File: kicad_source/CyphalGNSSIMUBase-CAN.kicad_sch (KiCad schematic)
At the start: 24 parts, among them CN1 RASPBERRYPI_PICO, CN2 SM04B-SRSS-TB, CN3 SM04B-SRSS-TB, SW1 PTS636 SM43 SMTR LFS, U3 M24C64-RMN6TP

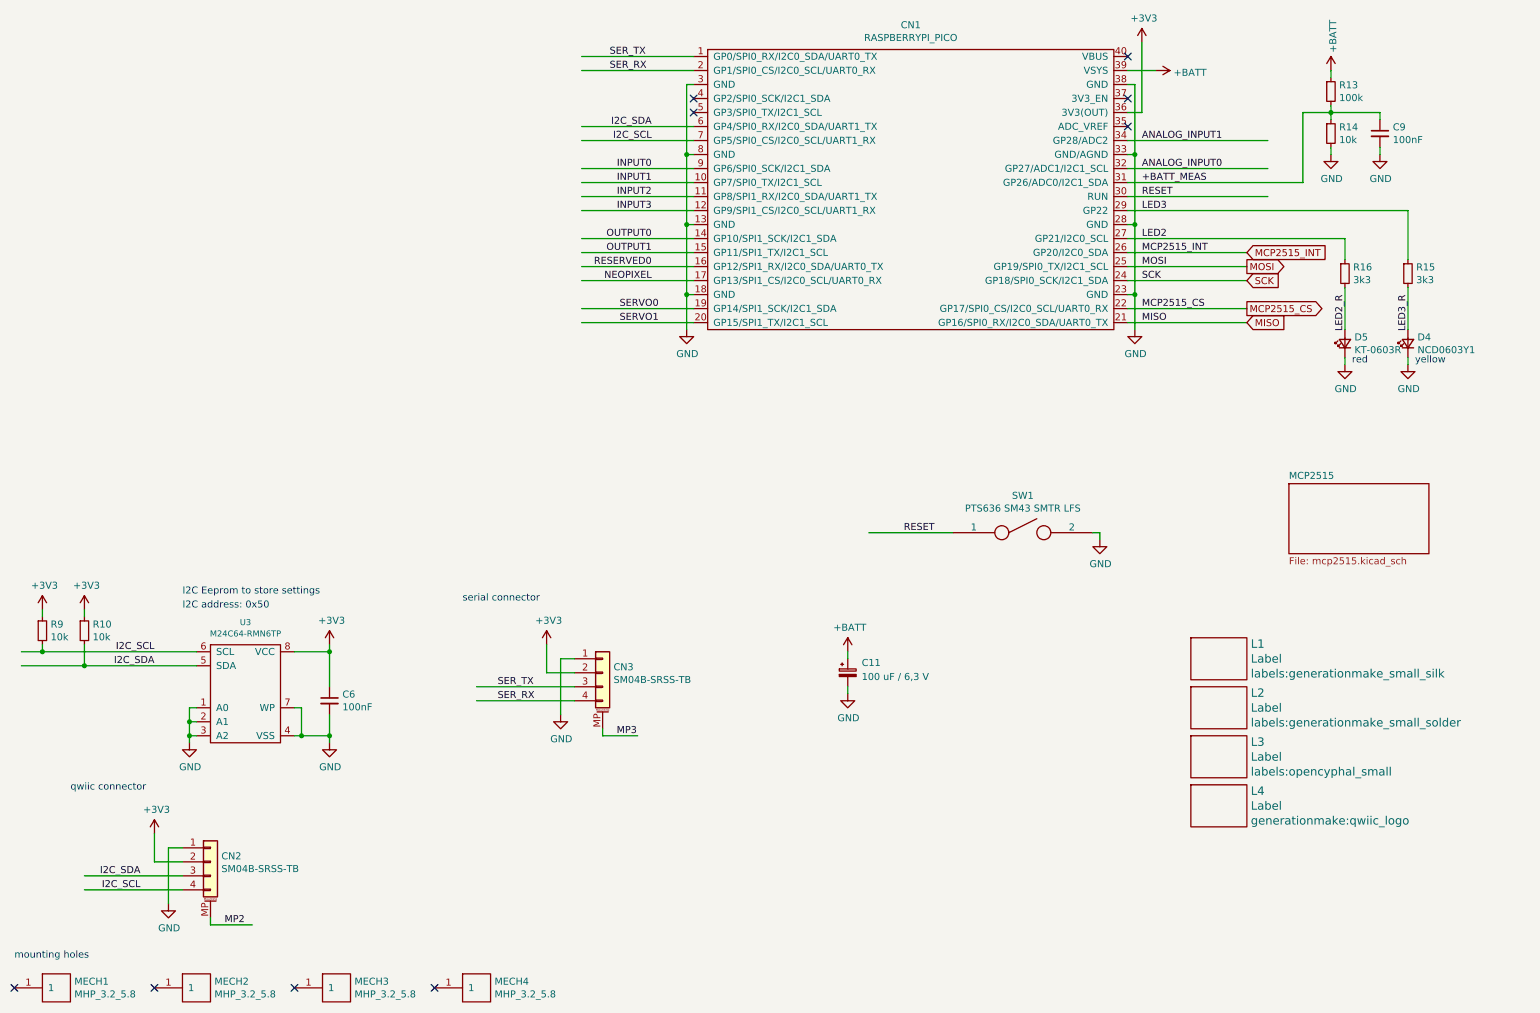
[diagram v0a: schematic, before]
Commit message: added BNO085
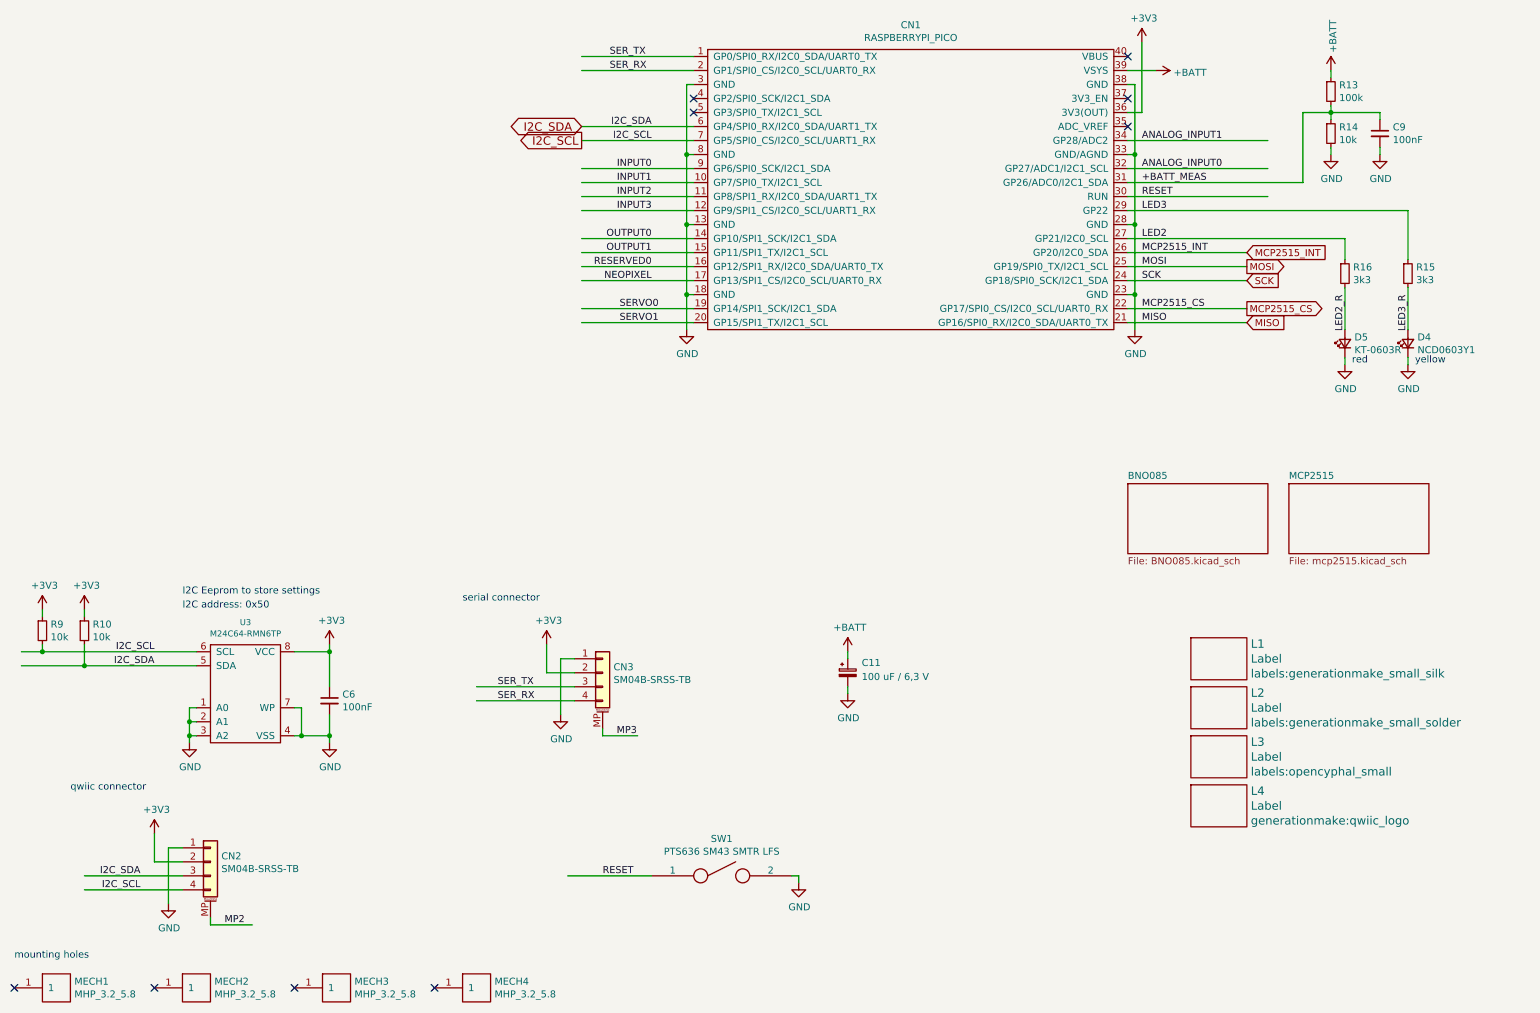
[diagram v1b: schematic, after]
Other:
- added sheet BNO085 (BNO085.kicad_sch)
- moved on the sheet: SW1
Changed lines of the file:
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@@
 	(wire
 		(pts
-			(xy 172.72 110.49) (xy 187.96 110.49)
+			(xy 118.11 172.72) (xy 133.35 172.72)
 		)
 		(stroke
@@
 	(wire
 		(pts
-			(xy 214.63 110.49) (xy 214.63 111.76)
+			(xy 160.02 172.72) (xy 160.02 173.99)
 		)
 		(stroke
@@
 	(wire
 		(pts
-			(xy 213.36 110.49) (xy 214.63 110.49)
+			(xy 158.75 172.72) (xy 160.02 172.72)
 		)
 		(stroke
@@
 	)
 	(label "RESET"
-		(at 179.07 110.49 0)
+		(at 124.46 172.72 0)
 		(effects
 			(font
@@
 		)
 	)
+	(global_label "I2C_SCL"
+		(shape output)
+		(at 120.65 39.37 180)
+		(fields_autoplaced yes)
+		(effects
+			(font
+				(size 1.524 1.524)
+			)
+			(justify right)
+		)
+		(property "Intersheetrefs" "${INTERSHEET_REFS}"
+			(at 108.7819 39.37 0)
+			(effects
+				(font
+					(size 1.27 1.27)
+				)
+				(justify right)
+				(hide yes)
+			)
+		)
+		(property "Referenzen zwischen Schaltplänen" "${INTERSHEET_REFS}"
+			(at 120.65 41.5721 0)
+			(effects
+				(font
+					(size 1.524 1.524)
+				)
+				(justify right)
+				(hide yes)
+			)
+		)
+	)
+	(global_label "I2C_SDA"
+		(shape bidirectional)
+		(at 120.65 36.83 180)
+		(fields_autoplaced yes)
+		(effects
+			(font
+				(size 1.524 1.524)
+			)
+			(justify right)
+		)
+		(property "Intersheetrefs" "${INTERSHEET_REFS}"
+			(at 107.5663 36.83 0)
+			(effects
+				(font
+					(size 1.27 1.27)
+				)
+				(justify right)
+				(hide yes)
+			)
+		)
+		(property "Referenzen zwischen Schaltplänen" "${INTERSHEET_REFS}"
+			(at 120.65 39.0321 0)
+			(effects
+				(font
+					(size 1.524 1.524)
+				)
+				(justify right)
+				(hide yes)
+			)
+		)
+	)
 	(global_label "MOSI"
 		(shape output)
@@
 	(symbol
 		(lib_id "OpenCyphalPicoBase-rescue:SPST-devices")
-		(at 200.66 110.49 0)
+		(at 146.05 172.72 0)
 		(unit 1)
 		(exclude_from_sim no)
@@
 		(dnp no)
 		(property "Reference" "SW1"
-			(at 200.66 103.759 0)
+			(at 146.05 165.989 0)
 			(effects
 				(font
@@
 		)
 		(property "Value" "PTS636 SM43 SMTR LFS"
-			(at 200.66 106.0704 0)
+			(at 146.05 168.3004 0)
 			(effects
 				(font
@@
 		)
 		(property "Footprint" "Button_Switch_SMD:SW_SPST_CK_RS282G05A3"
-			(at 200.66 110.49 0)
+			(at 146.05 172.72 0)
 			(effects
 				(font
@@
 		)
 		(property "Datasheet" ""
-			(at 200.66 110.49 0)
+			(at 146.05 172.72 0)
 			(effects
 				(font
@@
 		)
 		(property "Description" ""
-			(at 200.66 110.49 0)
+			(at 146.05 172.72 0)
 			(effects
 				(font
@@
 		)
 		(property "LCSC" "C2800965"
-			(at 200.66 110.49 0)
+			(at 146.05 172.72 0)
 			(effects
 				(font
@@
 	(symbol
 		(lib_id "OpenCyphalPicoBase-rescue:GND-power-supply")
-		(at 214.63 111.76 0)
+		(at 160.02 173.99 0)
 		(unit 1)
 		(exclude_from_sim no)
@@
 		(dnp no)
 		(property "Reference" "#PWR054"
-			(at 214.63 118.11 0)
+			(at 160.02 180.34 0)
 			(effects
 				(font
@@
 		)
 		(property "Value" "GND"
-			(at 214.757 116.1542 0)
+			(at 160.147 178.3842 0)
 			(effects
 				(font
@@
 		)
 		(property "Footprint" ""
-			(at 214.63 111.76 0)
+			(at 160.02 173.99 0)
 			(effects
 				(font
@@
 		)
 		(property "Datasheet" ""
-			(at 214.63 111.76 0)
+			(at 160.02 173.99 0)
 			(effects
 				(font
@@
 		)
 		(property "Description" ""
-			(at 214.63 111.76 0)
+			(at 160.02 173.99 0)
 			(effects
 				(font
@@
 				)
 			)
+		)
+	)
+	(sheet
+		(at 219.71 101.6)
+		(size 25.4 12.7)
+		(fields_autoplaced yes)
+		(stroke
+			(width 0)
+			(type solid)
+		)
+		(fill
+			(color 0 0 0 0.0000)
+		)
+		(property "Sheetname" "BNO085"
+			(at 219.71 100.8884 0)
+			(effects
+				(font
+					(size 1.27 1.27)
+				)
+				(justify left bottom)
+			)
+		)
+		(property "Sheetfile" "BNO085.kicad_sch"
+			(at 219.71 114.8846 0)
+			(effects
+				(font
+					(size 1.27 1.27)
+				)
+				(justify left top)
+			)
+		)
+		(instances
+			(project "CyphalGNSSIMUBase-CAN"
+				(path "/9d6d512e-1439-4aa2-b0d9-afb2dddd9146"
+					(page "3")
+				)
+			)

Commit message: added GNSS u-blox max-m10
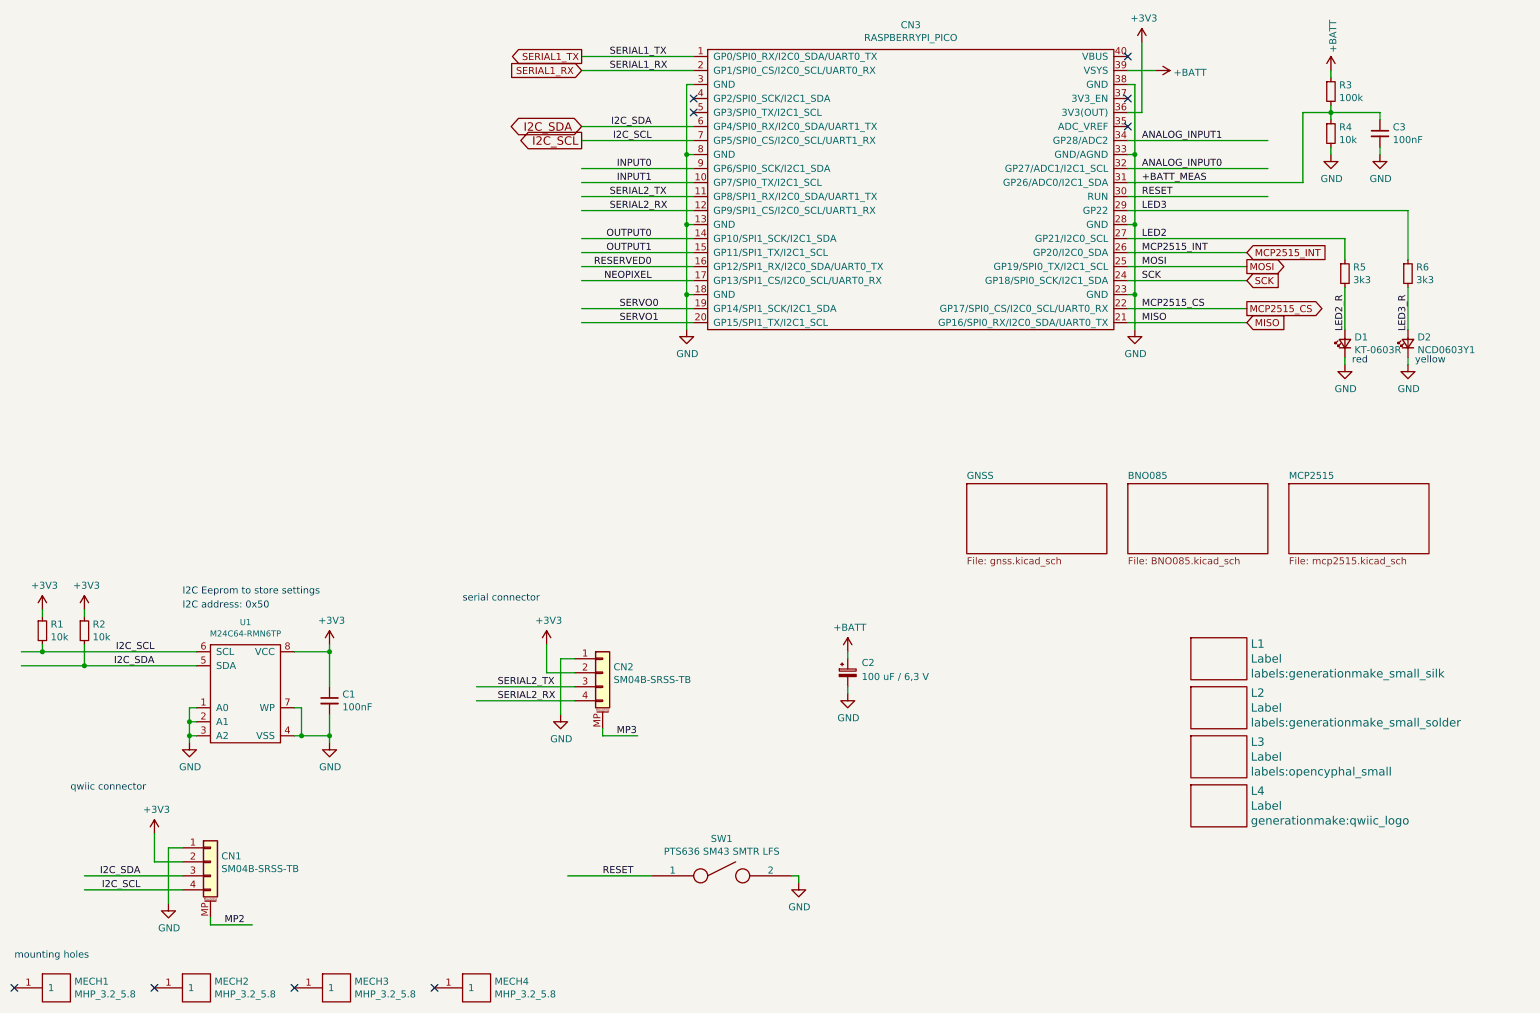
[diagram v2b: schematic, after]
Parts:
- renumbered C6 to C1, C11 to C2, C9 to C3, CN2 to CN1, CN3 to CN2, CN1 to CN3, D5 to D1, D4 to D2, R9 to R1, R10 to R2, R13 to R3, R14 to R4, R16 to R5, R15 to R6, U3 to U1
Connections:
- net INPUT2 renamed SERIAL2_TX
- net SERIAL2_TX: now also CN2.3 (Pin_3)
- net INPUT3 renamed SERIAL2_RX
- net SERIAL2_RX: now also CN2.4 (Pin_4)
- net SER_RX renamed SERIAL1_RX
- net SERIAL1_RX: no longer CN2.4 (Pin_4)
- net SER_TX renamed SERIAL1_TX
- net SERIAL1_TX: no longer CN2.3 (Pin_3)
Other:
- added sheet GNSS (gnss.kicad_sch)

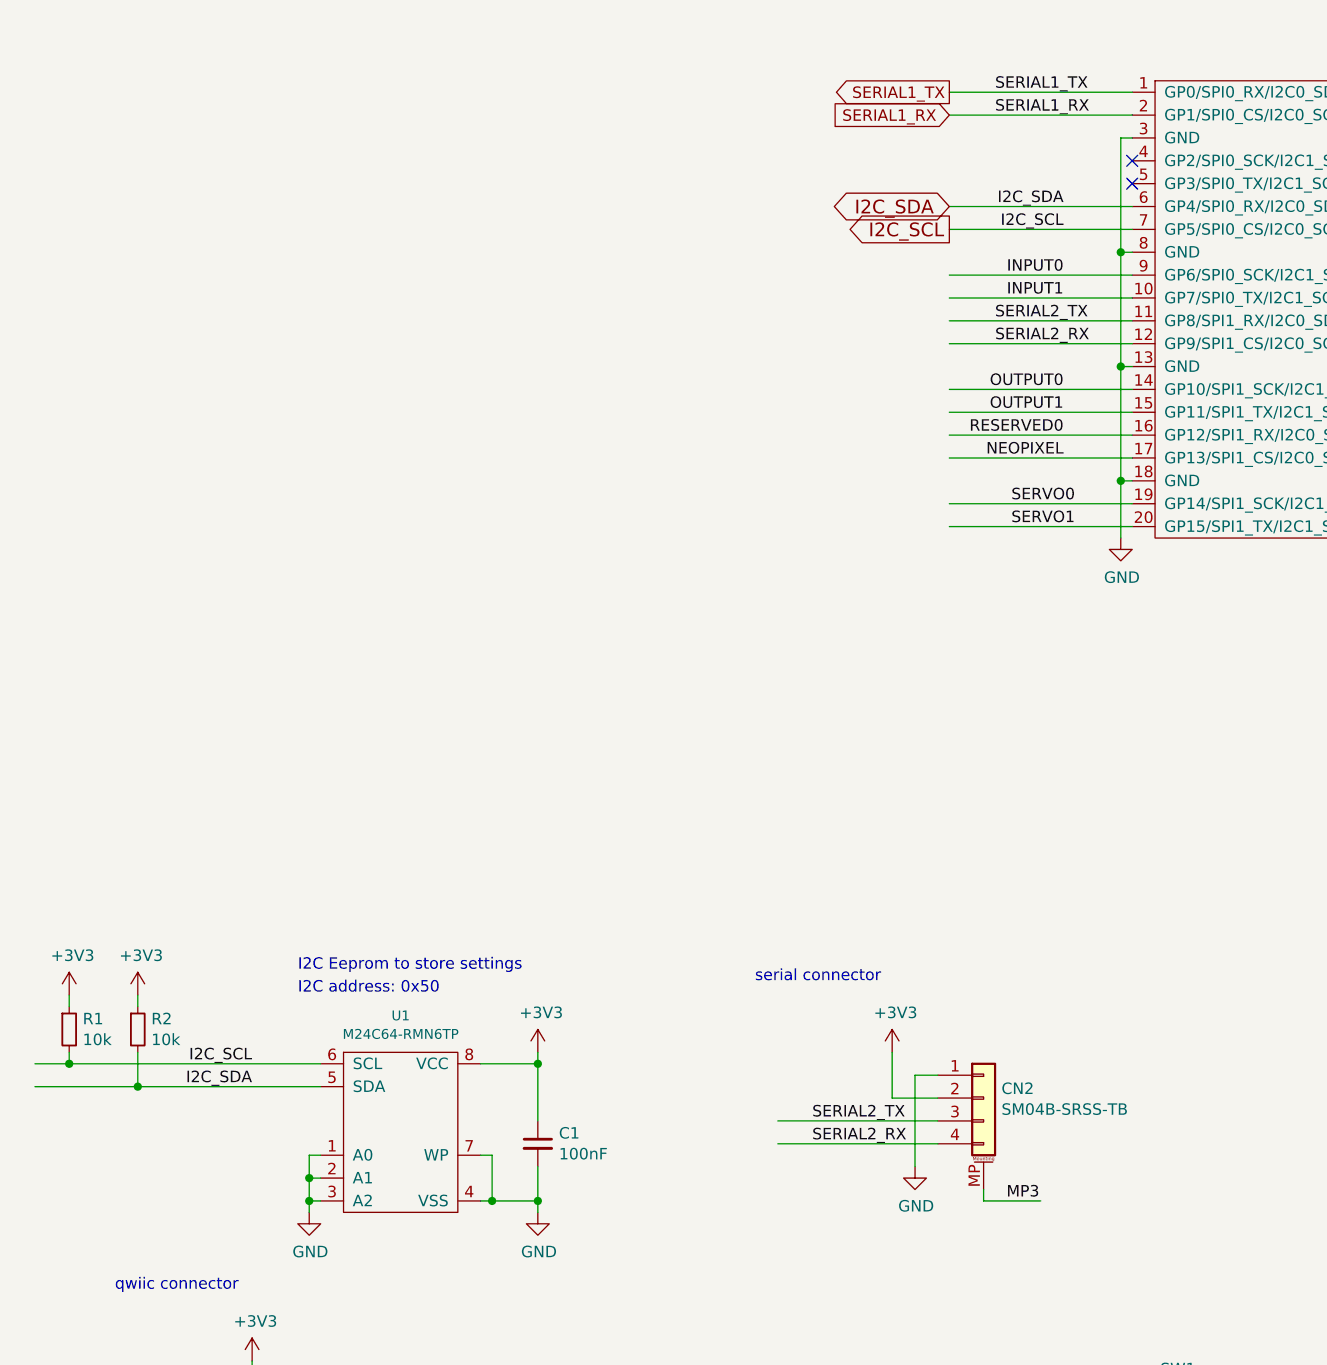
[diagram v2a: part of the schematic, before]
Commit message: added RS232 level shifter
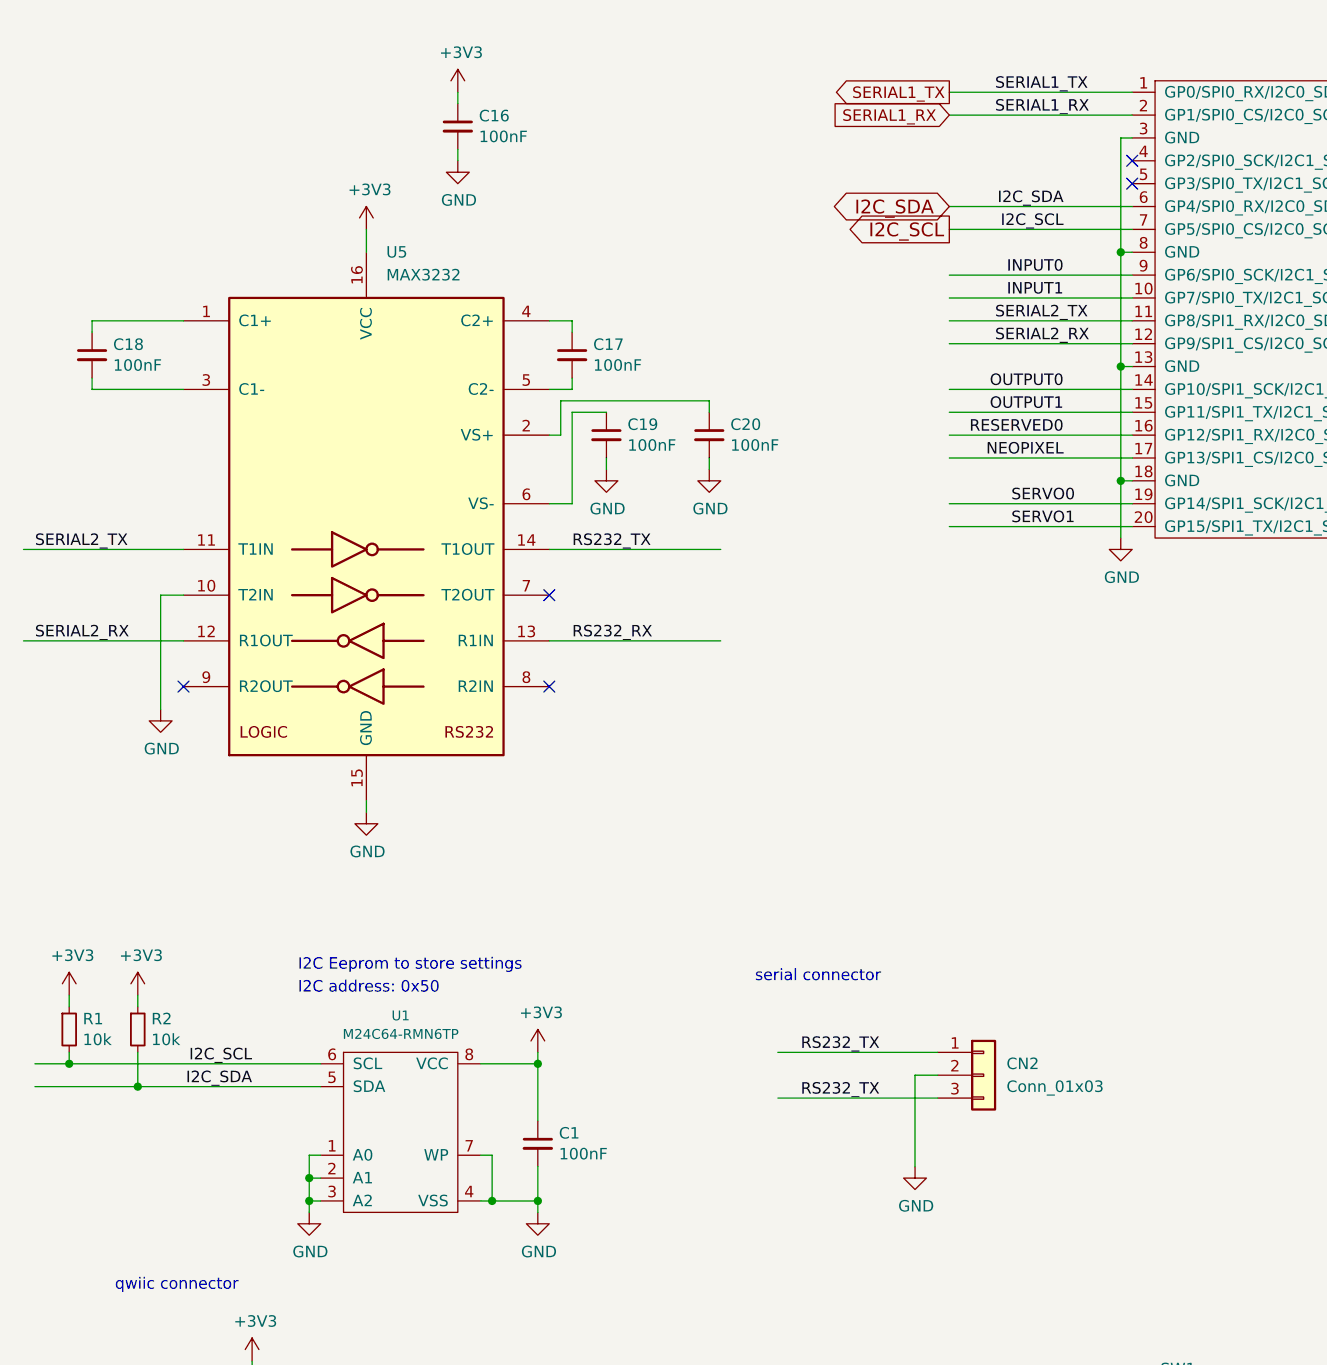
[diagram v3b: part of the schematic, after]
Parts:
- removed CN2: SM04B-SRSS-TB, generationmake:JST_SH_SM04B-SRSS-TB_1x04-1MP_P1.00mm_Horizontal, symbol Connector_Generic_MountingPin:Conn_01x04_MountingPin
- added C16, C17, C18, C19, C20: 100nF, Capacitor_SMD:C_0603_1608Metric, symbol Device:C_Small
- added CN2: Conn_01x03, Connector_JST:JST_EH_B3B-EH-A_1x03_P2.50mm_Vertical, symbol Connector_Generic:Conn_01x03
- added U5: MAX3232, Package_SO:SOIC-16_3.9x9.9mm_P1.27mm, symbol Interface_UART:MAX3232
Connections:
- net +3V3: now also C16.1, U5.16 (VCC)
- net GND: now also C16.2, C19.2, C20.2, CN2.2 (Pin_2), U5.10 (T2IN), U5.15 (GND)
- net SERIAL2_RX: now also U5.12 (R1OUT)
- net SERIAL2_TX: now also U5.11 (T1IN)
- new net: C20.1, U5.2 (VS+)
- new net: C19.1, U5.6 (VS-)
- new net: C18.1, U5.1 (C1+)
- new net: C18.2, U5.3 (C1-)
- new net: C17.1, U5.4 (C2+)
- new net: C17.2, U5.5 (C2-)
- new net RS232_RX: U5.13 (R1IN)
- new net RS232_TX: CN2.1 (Pin_1), CN2.3 (Pin_3), U5.14 (T1OUT)
- no-connect marks 9 -> 12
